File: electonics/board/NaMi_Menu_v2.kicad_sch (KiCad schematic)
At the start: 20 parts, among them J3 Conn_01x07, J5 Conn_02x08_Odd_Even, U2 RP2305

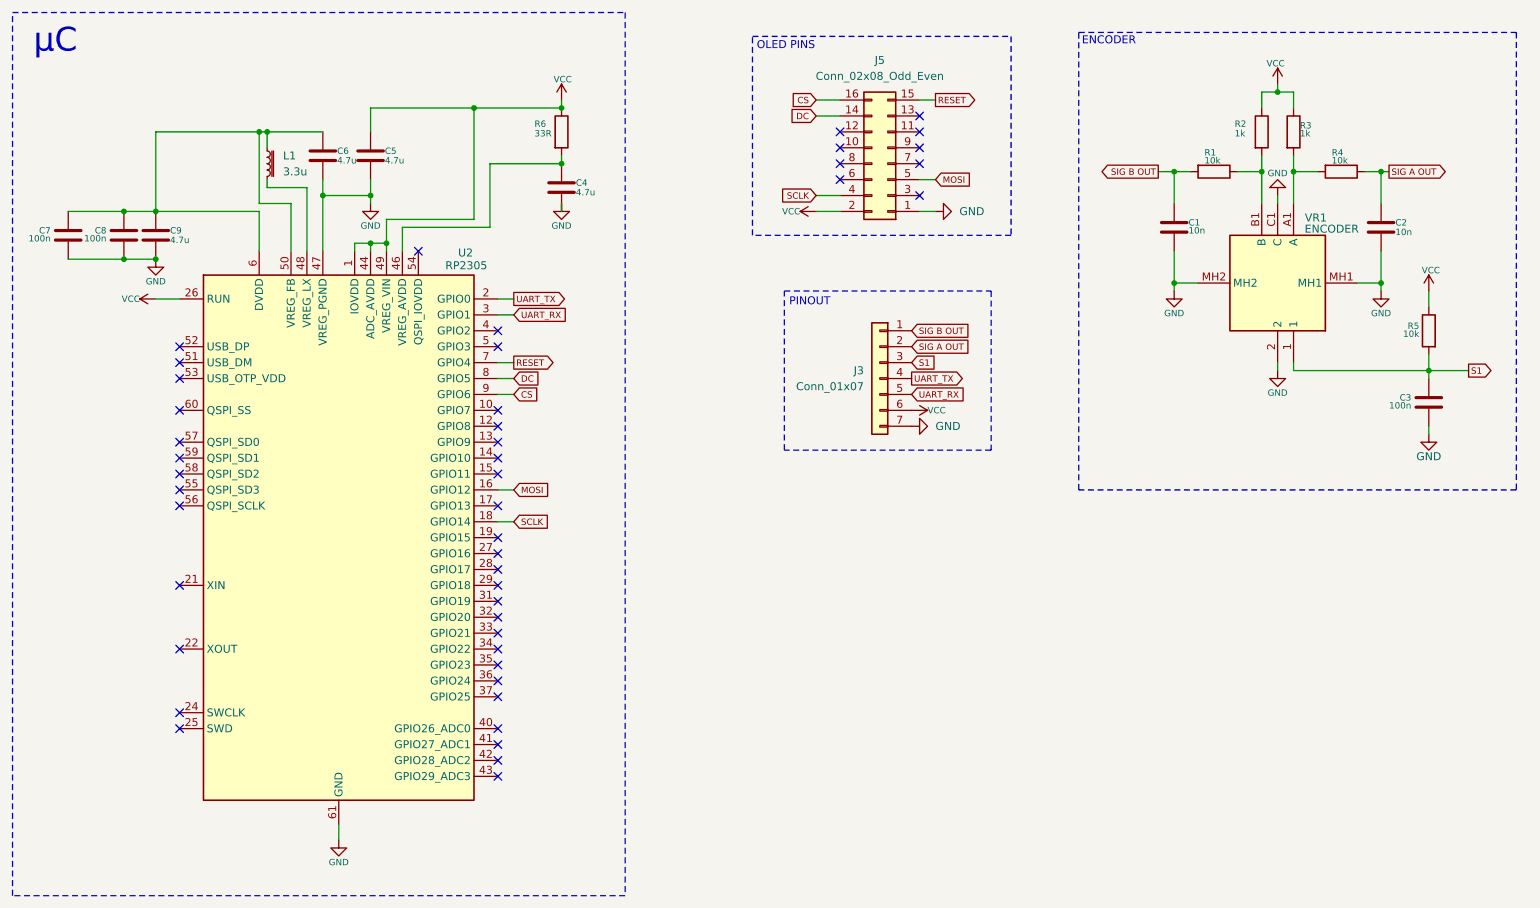
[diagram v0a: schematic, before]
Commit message: schemat wersja z SPI
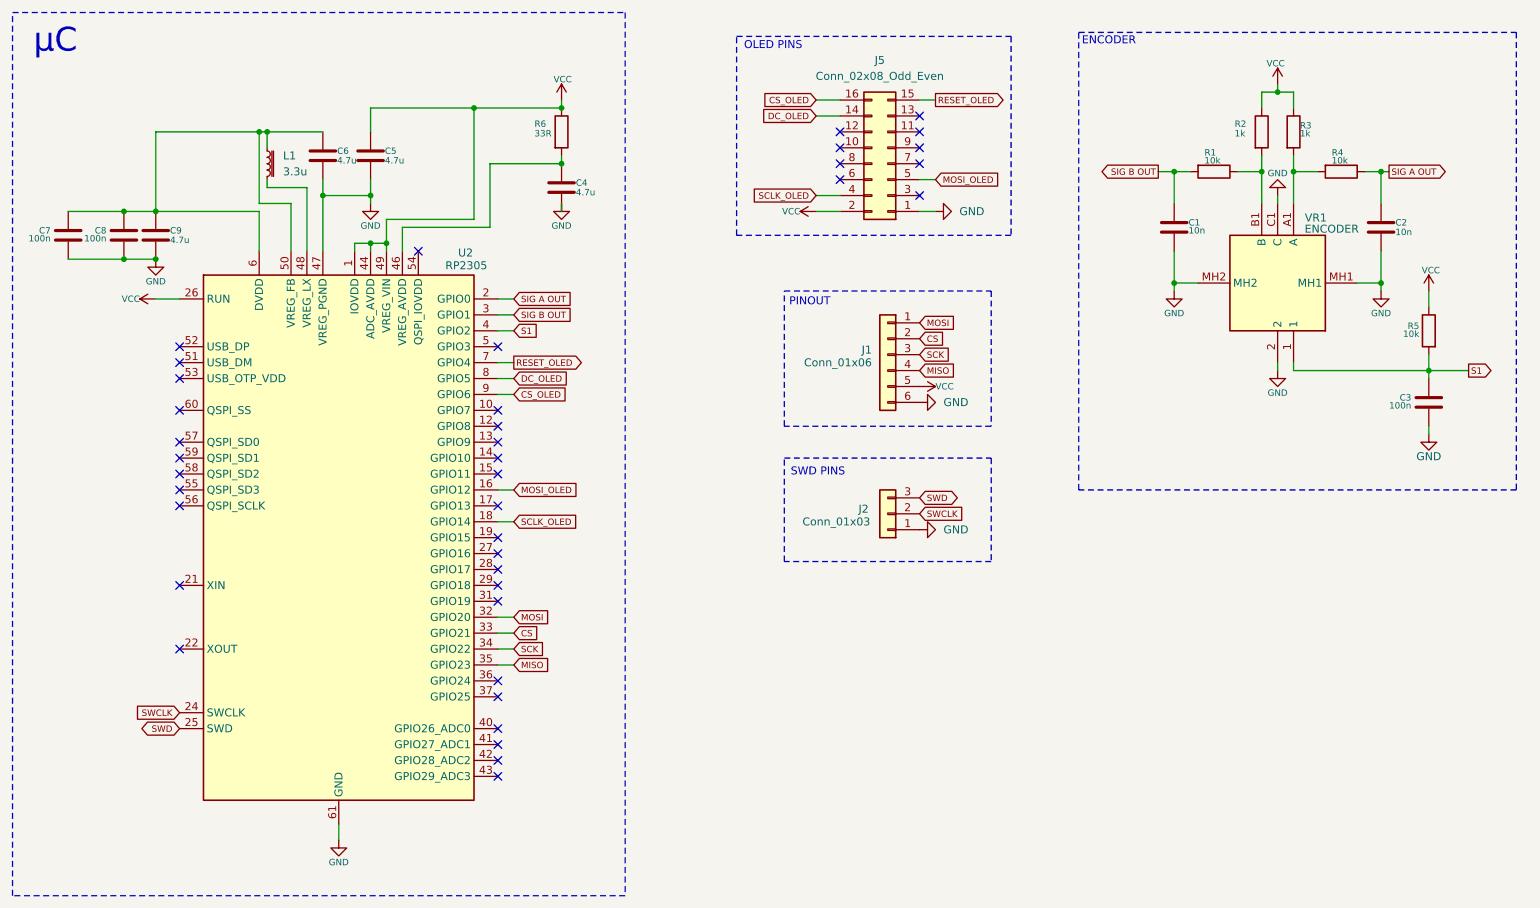
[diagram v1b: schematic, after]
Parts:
- removed J3: Conn_01x07, symbol Connector_Generic:Conn_01x07
- added J1: Conn_01x06, symbol Connector_Generic:Conn_01x06
- added J2: Conn_01x03, symbol Connector_Generic:Conn_01x03
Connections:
- net UART_RX is gone; now on net SIG B OUT: U2.3 (GPIO1)
- net UART_TX is gone; now on net SIG A OUT: U2.2 (GPIO0)
- net CS: now also U2.33 (GPIO21), J1.2 (Pin_2); no longer J5.16 (Pin_16), U2.9 (GPIO6)
- net GND: now also J1.6 (Pin_6), J2.1 (Pin_1)
- net MOSI: now also U2.32 (GPIO20), J1.1 (Pin_1); no longer J5.5 (Pin_5), U2.16 (GPIO12)
- net S1: now also U2.4 (GPIO2)
- net VCC: now also J1.5 (Pin_5)
- net SWCLK: now reaches U2.24 (SWCLK)
- net SWCLK: now also J2.2 (Pin_2)
- net SWD: now reaches U2.25 (SWD)
- net SWD: now also J2.3 (Pin_3)
- net SCK: now reaches U2.34 (GPIO22)
- net SCK: now also J1.3 (Pin_3)
- net MISO: now reaches U2.35 (GPIO23)
- net MISO: now also J1.4 (Pin_4)
- net DC renamed DC_OLED
- net RESET renamed RESET_OLED
- net SCLK renamed SCLK_OLED
- new net CS_OLED: J5.16 (Pin_16), U2.9 (GPIO6)
- new net MOSI_OLED: J5.5 (Pin_5), U2.16 (GPIO12)
- no-connect marks 46 -> 39
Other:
- note added: "SWD PINS"

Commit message: Schemat wersja z Interrupt
Dodano wyjście interrupt, 5 miejsc na przyciski oraz 5 miejsc na diody LED.  Dodano również LED sygnalizacyjny na zasilaniu.
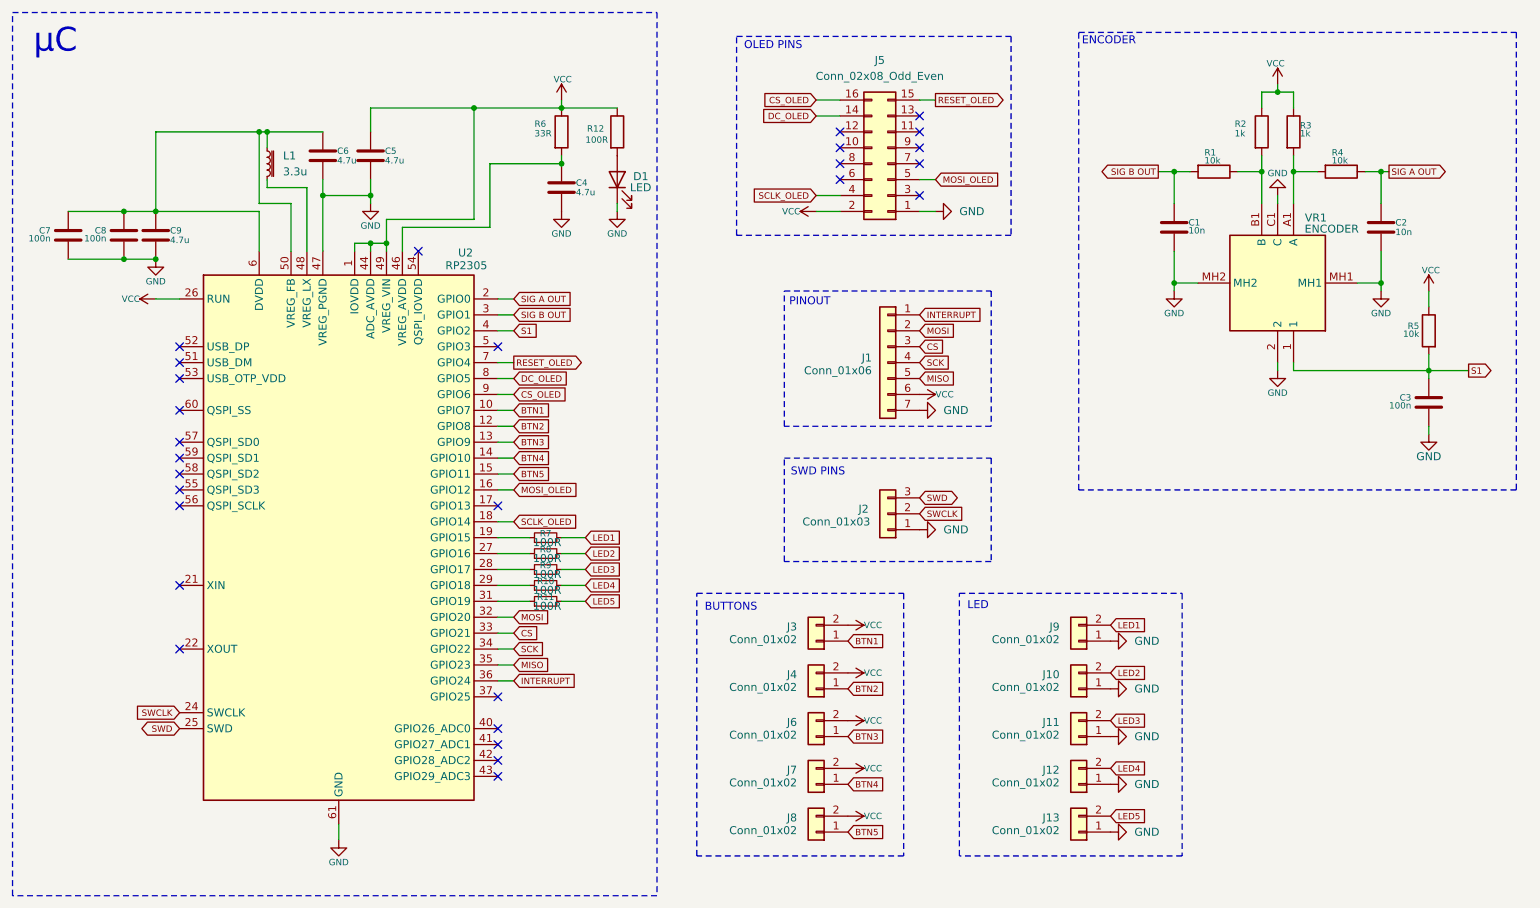
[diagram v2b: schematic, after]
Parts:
- added D1: LED, symbol Device:LED
- added J10, J11, J12, J13, J3, J4, J6, J7, J8, J9: Conn_01x02, symbol Connector_Generic:Conn_01x02
- added R10, R11, R7, R8, R9: 100R, symbol Device:R_Small
- added R12: 100R, Resistor_SMD:R_0402_1005Metric, symbol Device:R
- J1: symbol Connector_Generic:Conn_01x06 -> Connector_Generic:Conn_01x07
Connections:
- net CS: now also J1.3 (Pin_3); no longer J1.2 (Pin_2)
- net GND: now also J1.7 (Pin_7), D1.1 (K), J10.1 (Pin_1), J11.1 (Pin_1), J12.1 (Pin_1), J13.1 (Pin_1), J9.1 (Pin_1); no longer J1.6 (Pin_6)
- net MISO: now also J1.5 (Pin_5); no longer J1.4 (Pin_4)
- net MOSI: now also J1.2 (Pin_2); no longer J1.1 (Pin_1)
- net SCK: now also J1.4 (Pin_4); no longer J1.3 (Pin_3)
- net VCC: now also J1.6 (Pin_6), J3.2 (Pin_2), J4.2 (Pin_2), J6.2 (Pin_2), J7.2 (Pin_2), J8.2 (Pin_2), R12.1; no longer J1.5 (Pin_5)
- net BTN1: now reaches U2.10 (GPIO7)
- net BTN1: now also J3.1 (Pin_1)
- net BTN2: now reaches U2.12 (GPIO8)
- net BTN2: now also J4.1 (Pin_1)
- net BTN3: now reaches U2.13 (GPIO9)
- net BTN3: now also J6.1 (Pin_1)
- net BTN4: now reaches U2.14 (GPIO10)
- net BTN4: now also J7.1 (Pin_1)
- net BTN5: now reaches U2.15 (GPIO11)
- net BTN5: now also J8.1 (Pin_1)
- net at U2.19 (GPIO15): now also R7.1
- net at U2.27 (GPIO16): now also R8.1
- net at U2.28 (GPIO17): now also R9.1
- net at U2.29 (GPIO18): now also R10.1
- net at U2.31 (GPIO19): now also R11.1
- net INTERRUPT: now reaches U2.36 (GPIO24)
- net INTERRUPT: now also J1.1 (Pin_1)
- new net: D1.2 (A), R12.2
- new net LED1: J9.2 (Pin_2), R7.2
- new net LED2: J10.2 (Pin_2), R8.2
- new net LED3: J11.2 (Pin_2), R9.2
- new net LED4: J12.2 (Pin_2), R10.2
- new net LED5: J13.2 (Pin_2), R11.2
- no-connect marks 39 -> 28
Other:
- note added: "BUTTONS"
- note added: "LED"

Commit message: v2 board with MC
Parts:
- added H1, H2, H3, H4, H5, H6: MountingHole, MountingHole:MountingHole_3.2mm_M3, symbol Mechanical:MountingHole
- C1, C2, C3, C4, C5, C6, C7, C8, C9: footprint Capacitor_SMD:C_0402_1005Metric -> Capacitor_SMD:C_0805_2012Metric
- D1: footprint (none) -> LED_SMD:LED_0805_2012Metric
- J1: footprint (none) -> Connector_PinHeader_2.54mm:PinHeader_1x07_P2.54mm_Vertical
- J10, J11, J12, J13, J3, J4, J6, J7, J8, J9: footprint (none) -> Connector_PinHeader_2.54mm:PinHeader_1x02_P2.54mm_Vertical
- J2: footprint (none) -> Connector_PinHeader_2.54mm:PinHeader_1x03_P2.54mm_Vertical
- L1: footprint (none) -> Inductor_SMD:L_0805_2012Metric
- R1, R12, R2, R3, R4, R5, R6: footprint Resistor_SMD:R_0402_1005Metric -> Resistor_SMD:R_0805_2012Metric
- R10, R11, R7, R8, R9: footprint (none) -> Resistor_SMD:R_0805_2012Metric
- U2: footprint (none) -> Package_DFN_QFN:QFN-60-1EP_7x7mm_P0.4mm_EP3.4x3.4mm
- VR1: footprint PEC11R4220FS0024 -> PEC:PEC11R4220FS0024
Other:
- note added: "Mounting Holes M3"

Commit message: Modified PCB design
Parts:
- removed H2, H3: MountingHole, MountingHole:MountingHole_3.2mm_M3, symbol Mechanical:MountingHole
- L1: footprint Inductor_SMD:L_0805_2012Metric -> Inductor_SMD:L_Neosid_SMs42
- R10, R11, R12, R7, R8, R9: value 100R -> 1k
- renumbered H4 to H2, H5 to H3, H6 to H4, J5 to J2, J2 to J3, J3 to J4, J4 to J5
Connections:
- net BTN1: now also J4.2 (Pin_2); no longer J4.1 (Pin_1)
- net BTN2: now also J5.2 (Pin_2); no longer J5.1 (Pin_1)
- net BTN3: now also J6.2 (Pin_2); no longer J6.1 (Pin_1)
- net BTN4: now also J7.2 (Pin_2); no longer J7.1 (Pin_1)
- net BTN5: now also J8.2 (Pin_2); no longer J8.1 (Pin_1)
- net GND: now also J4.1 (Pin_1), J5.1 (Pin_1), J6.1 (Pin_1), J7.1 (Pin_1), J8.1 (Pin_1)
- net VCC: no longer J4.2 (Pin_2), J5.2 (Pin_2), J6.2 (Pin_2), J7.2 (Pin_2), J8.2 (Pin_2)
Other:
- moved on the sheet: H2, H3, H4
